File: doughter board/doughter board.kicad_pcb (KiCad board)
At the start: 2 copper layers, 36 parts, among them J1 BOOT_TO/ SELECTOR, J2 BOOT_TO/ SELECTOR, J3 Conn_01x05, J4 RS485, J5 UART2, SW1 SW_SPST, U1 LM1117-3.3, U2 SN65HVD11, U3 STM32F030C6Tx, Y1 8 MHz

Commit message: time is just a number
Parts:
- moved C7 93.6 mm to (163.2, 77.1)
- moved R6 87.0 mm to (165.5, 73.3), turned to -90 degrees
- moved R5 84.8 mm to (162.5, 73.0), turned to -90 degrees
- moved J3 84.1 mm to (147.3, 58.4), turned to 90 degrees
- moved C8 83.7 mm to (158.3, 63.5)
- moved R4 82.7 mm to (160.0, 71.1), turned to 90 degrees
- moved R12 81.6 mm to (166.2, 68.4), turned to 90 degrees
- moved R8 80.1 mm to (158.4, 76.2)
- moved R11 79.7 mm to (163.7, 68.4), turned to 90 degrees
- moved C9 78.1 mm to (153.3, 63.5)
- moved U1 77.7 mm to (165.1, 61.0)
- moved R9 77.2 mm to (160.0, 67.0), turned to 90 degrees
- moved C3 75.7 mm to (144.8, 68.7), turned to -90 degrees
- moved C10 72.6 mm to (148.2, 63.5)
- moved R2 66.0 mm to (141.2, 69.2), turned to -90 degrees
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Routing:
- net +3.3V: track 0.00 -> 42.5 mm
- net GND: track 0.00 -> 26.0 mm
- net RST: track 0.00 -> 15.6 mm, vias 0 -> 1
- net SWD_O: track 0.00 -> 13.2 mm, vias 0 -> 1
- net SWD_CLK: track 0.00 -> 12.9 mm, vias 0 -> 1
- net +5V: track 10.7 -> 0.00 mm
- net /UART2_TX: track 1.00 -> 0.00 mm
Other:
- board outline added: 61 x 27.9 mm

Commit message: PCB doughter - layout
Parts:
- moved D1 44.3 mm to (157.5, 58.4)
- moved C2 44.3 mm to (161.3, 66.0), turned to 90 degrees
- moved C5 44.1 mm to (158.4, 73.2), turned to -90 degrees
- moved J2 37.6 mm to (151.1, 66.0)
- moved C1 36.3 mm to (158.3, 64.7), turned to 90 degrees
- moved J3 34.4 mm to (113.0, 55.5)
- moved C8 33.9 mm to (124.5, 62.2)
- moved C7 33.8 mm to (137.2, 55.5), turned to 180 degrees
- moved C9 32.8 mm to (120.7, 59.7)
- moved R2 29.5 mm to (111.8, 67.3)
- moved D3 28.8 mm to (146.1, 67.3), turned to -90 degrees
- moved J4 28.7 mm to (163.8, 58.4), turned to 180 degrees
- moved R12 27.2 mm to (139.7, 62.2), turned to 180 degrees
- moved R8 25.8 mm to (139.7, 58.4), turned to 90 degrees
- moved R3 24.8 mm to (150.4, 57.9), turned to -90 degrees
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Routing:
- net +3.3V: track 42.5 -> 120.1 mm
- net GND: track 26.0 -> 1.43 mm
- net DE: track 0.00 -> 23.1 mm, vias 0 -> 2
- net RST: track 15.6 -> 38.1 mm
- net ~{RE}: track 0.00 -> 19.6 mm, vias 0 -> 2
- net UART1_RX_R: track 0.00 -> 19.1 mm, vias 0 -> 4
- net /A: track 0.00 -> 18.4 mm
- net Xtal_IN: track 0.00 -> 14.8 mm
- net UART1_TX_D: track 0.00 -> 12.4 mm, vias 0 -> 2
- net /B: track 0.00 -> 12.1 mm
- net SWD_O: track 13.2 -> 25.1 mm
- net Xtal_OUT: track 0.00 -> 11.1 mm
- net +5V: track 0.00 -> 10.2 mm
- net SWD_CLK: track 12.9 -> 22.2 mm
- net Net-(U2-B): track 0.00 -> 8.62 mm
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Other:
- board size 61 x 27.9 mm -> 58.4 x 24.1 mm

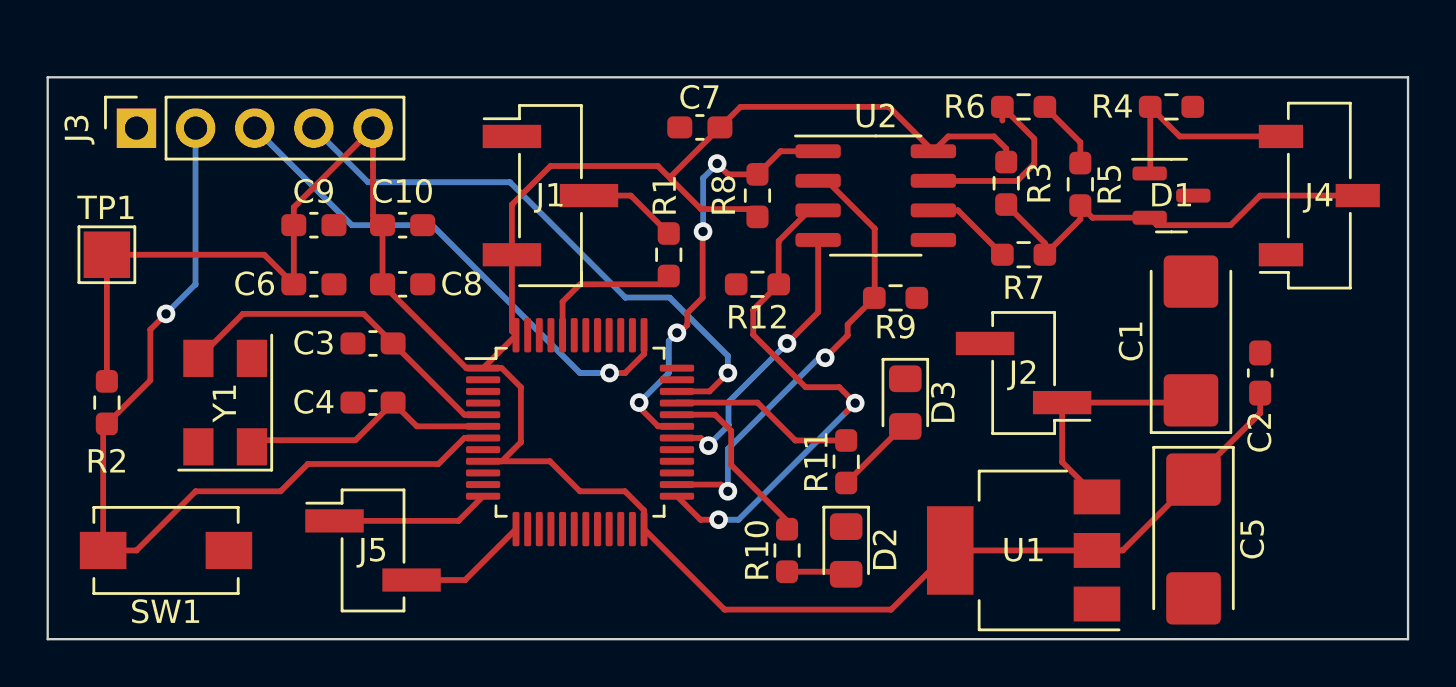
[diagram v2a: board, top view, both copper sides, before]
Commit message: doughter PCB - with no GND connection
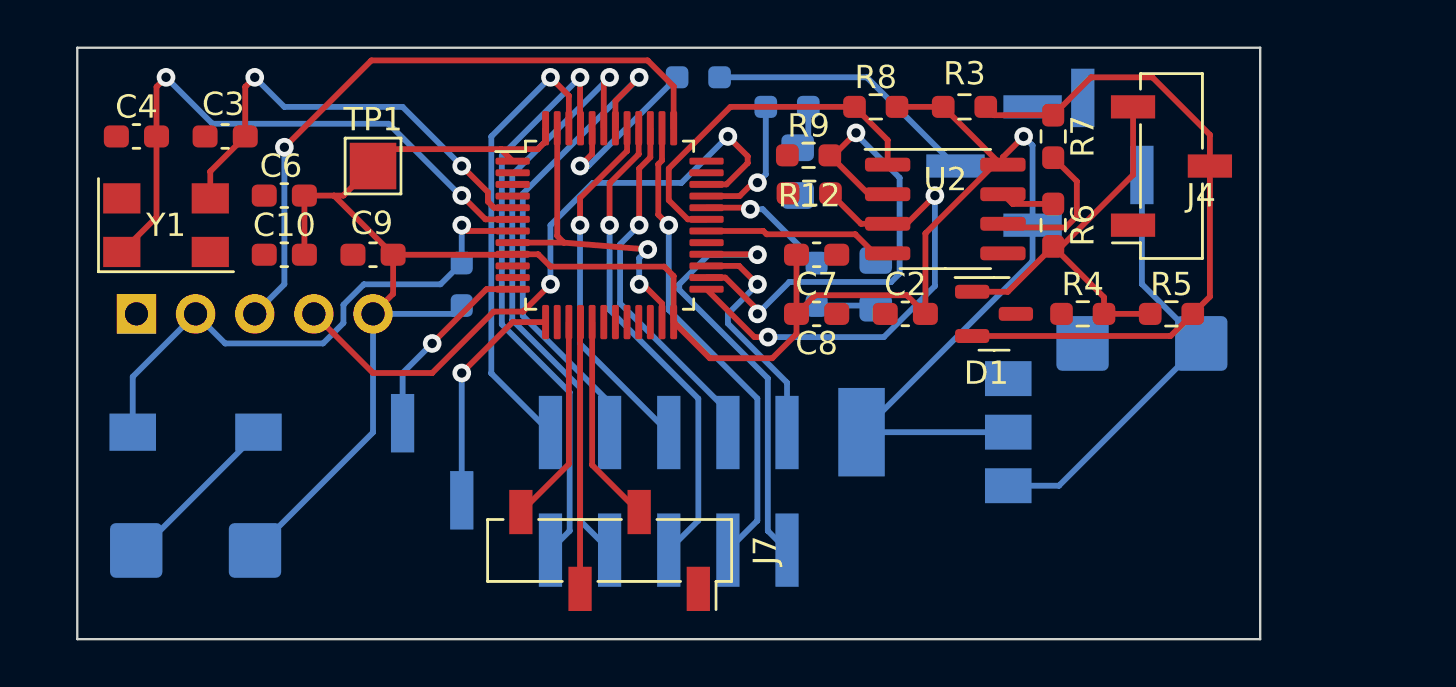
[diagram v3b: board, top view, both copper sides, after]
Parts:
- added J6: INPUT, Connector_PinHeader_2.54mm:PinHeader_2x05_P2.54mm_Vertical_SMD, B.Cu at (135.9, 71.1)
- added J7: Serial_BUS, Connector_PinSocket_2.54mm:PinSocket_1x04_P2.54mm_Vertical_SMD_Pin1Right, F.Cu at (133.3, 73.7)
- C1, C5, D2, D3, J1, J2, J3, J5, R1, R10, R11, R2, SW1, U1: moved to B.Cu
- moved C5 42.9 mm to (115.6, 73.7), turned to 180 degrees
- moved J1 19.1 mm to (149.9, 57.1), turned to 180 degrees
- moved C8 17.8 mm to (142.2, 63.5)
- moved R2 16.1 mm to (127.0, 62.2), turned to 90 degrees
- moved R11 15.5 mm to (141.0, 54.6), turned to 0 degrees
- moved C2 15.5 mm to (146.1, 63.5), turned to 180 degrees
- moved C4 15.3 mm to (113.0, 55.9)
- moved TP1 12.0 mm to (123.2, 57.1)
- moved D2 11.5 mm to (144.8, 62.2)
- moved R10 11.5 mm to (142.2, 62.2)
- moved D3 10.9 mm to (141.4, 57.4), turned to 90 degrees
- moved C3 10.9 mm to (116.8, 55.9)
- moved J2 10.9 mm to (154.9, 55.9), turned to 90 degrees
- moved R4 9.67 mm to (153.7, 63.5), turned to 180 degrees
- moved D1 9.16 mm to (149.9, 63.5)
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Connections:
- U3 pad 23: unconnected-(U3-VSS-Pad23) -> Net-(U3-VSSA)
- U3 pad 47: unconnected-(U3-VSS-Pad47) -> Net-(U3-VSSA)
- U3 pad 8: unconnected-(U3-VSSA-Pad8) -> Net-(U3-VSSA)
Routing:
- net /Col1: track 0.00 -> 26.1 mm, vias 0 -> 1
- net /Col2: track 0.00 -> 25.5 mm, vias 0 -> 1
- net /Col0: track 0.00 -> 21.5 mm, vias 0 -> 1
- net /Col4: track 0.00 -> 20.7 mm, vias 0 -> 1
- net /Col7: track 0.00 -> 20.5 mm, vias 0 -> 1
- net /Col3: track 0.00 -> 19.9 mm, vias 0 -> 1
- net /Col9: track 0.00 -> 19.4 mm, vias 0 -> 1
- net /Col6: track 0.00 -> 16.6 mm, vias 0 -> 1
- net /Col5: track 0.00 -> 15.5 mm, vias 0 -> 1
- net Xtal_OUT: track 11.1 -> 25.9 mm, vias 0 -> 2
- net Net-(U3-VSSA): track 0.00 -> 14.6 mm, vias 0 -> 2
- net +3.3V: track 120.1 -> 105.6 mm, vias 0 -> 1
- net RST: track 38.1 -> 24.0 mm
- net /S_LE: track 0.00 -> 11.5 mm
- net /A: track 18.4 -> 29.3 mm
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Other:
- board size 58.4 x 24.1 mm -> 50.8 x 25.4 mm

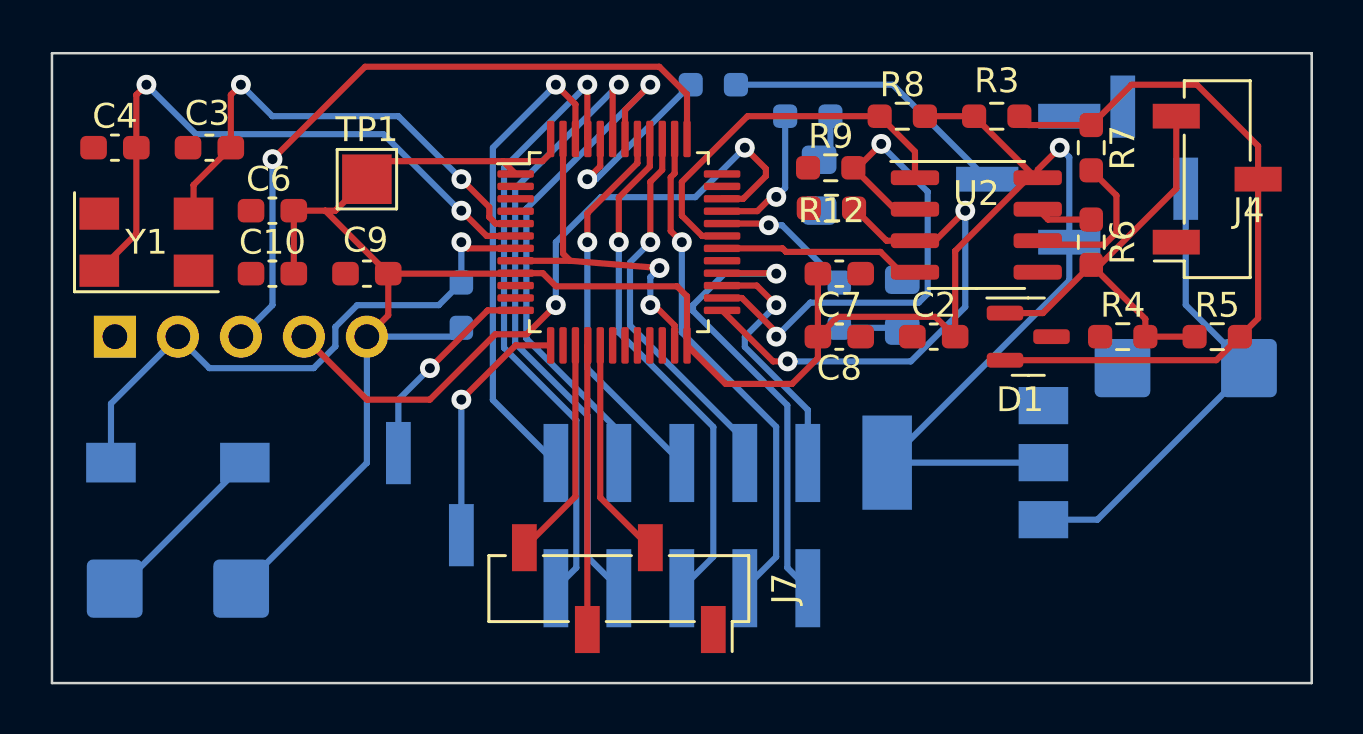
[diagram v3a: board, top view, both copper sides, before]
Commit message: Modified layout, filled GND planes, added info on silkscreen
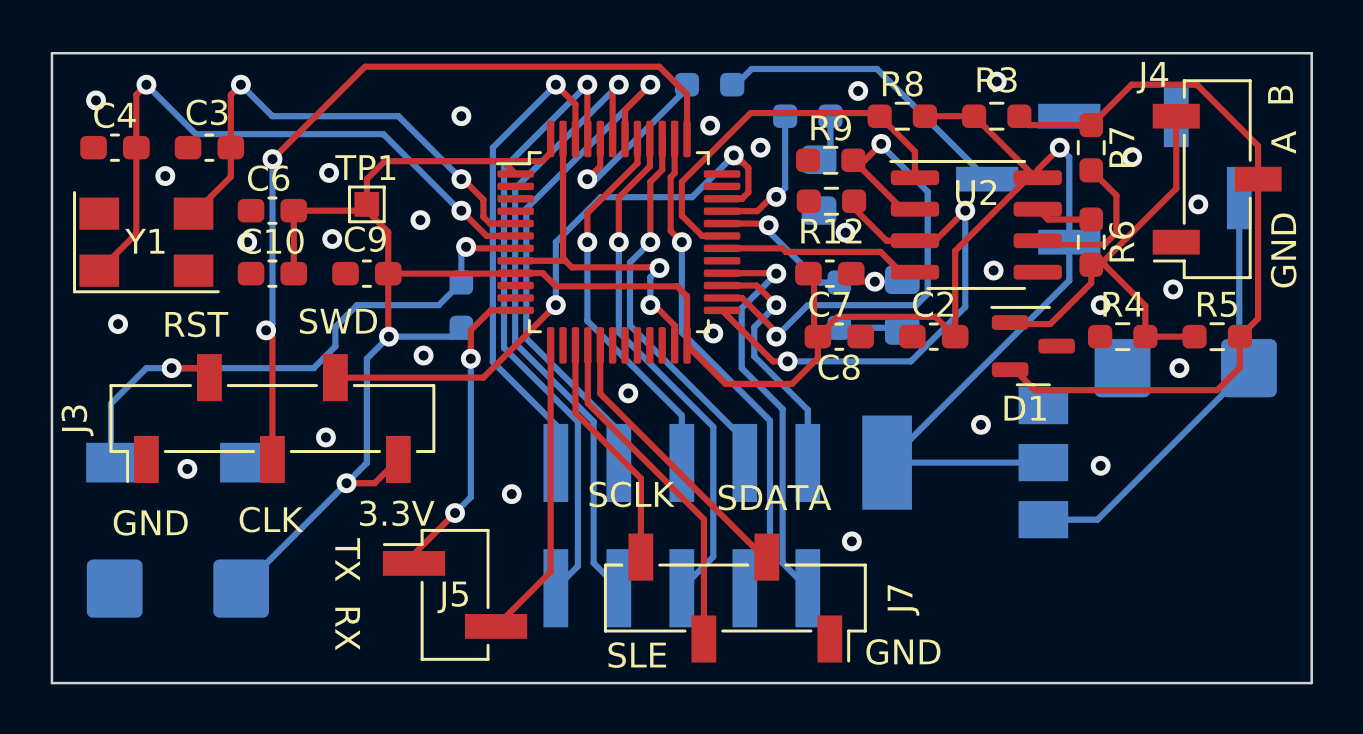
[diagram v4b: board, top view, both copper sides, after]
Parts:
- J3: footprint Connector_PinSocket_2.54mm:PinSocket_1x05_P2.54mm_Vertical -> Connector_PinSocket_2.54mm:PinSocket_1x05_P2.54mm_Vertical_SMD_Pin1Left; moved to F.Cu
- J5: moved to F.Cu
- J6: value INPUT -> OUTPUT
- TP1: footprint TestPoint:TestPoint_Pad_2.0x2.0mm -> TestPoint:TestPoint_Pad_1.0x1.0mm
- moved J3 7.16 mm to (119.4, 66.8), turned to 90 degrees
- moved J7 4.71 mm to (138.0, 74.0)
- moved J5 4.19 mm to (126.7, 73.9), turned to 0 degrees
- moved J2 2.19 mm to (157.1, 56.3)
- moved TP1 1.02 mm to (123.2, 58.2)
- moved D1 0.43 mm to (150.1, 63.9)
- moved C7 0.38 mm to (141.9, 61.0)
- moved R9 0.30 mm to (141.9, 56.4)
- moved R12 0.28 mm to (141.9, 58.0)
- moved R1 0.15 mm to (137.0, 53.3)
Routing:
- net GND: track 7.35 -> 1.82 mm, vias 0 -> 29
- net SWD_CLK: track 28.2 -> 32.8 mm, vias 1 -> 2
- net /UART2_TX: track 8.37 -> 12.5 mm, vias 1 -> 2
- net SWD_O: track 28.2 -> 24.4 mm
- net /Col9: track 19.4 -> 16.6 mm
- net /S_DATA: track 8.99 -> 11.4 mm
- net /S_LE: track 11.5 -> 13.8 mm
- net /UART2_RX: track 9.97 -> 12.2 mm, vias 1 -> 0
- net +3.3V: track 105.6 -> 107.4 mm, vias 1 -> 3
- net +5V: track 19.1 -> 17.8 mm
- net /A: track 29.3 -> 30.5 mm
- net /S_CLK: track 9.01 -> 9.63 mm
- net Net-(J1-Pin_2): track 11.7 -> 12.2 mm
- net RST: track 24.0 -> 24.2 mm, vias 1 -> 2
- added copper zone on B.Cu, net GND
- added copper zone on F.Cu, net GND
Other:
- board text added: "1"
- board text added: "10"
- board text added: "2"
- board text added: "3"
- board text added: "3.3V"
- board text added: "4"
- board text added: "5"
- board text added: "5V"
- board text added: "6"
- board text added: "7"
- board text added: "8"
- board text added: "9"
- board text added: "A"
- board text added: "B"
- board text added: "BOOT0"
- board text added: "CLK"
- board text added: "COLUMNS"
- board text added: "GND"
- board text added: "RST"
- board text added: "RX"
- board text added: "SCLK"
- board text added: "SDATA"
- board text added: "SLE"
- board text added: "SWD"
- board text added: "TX"

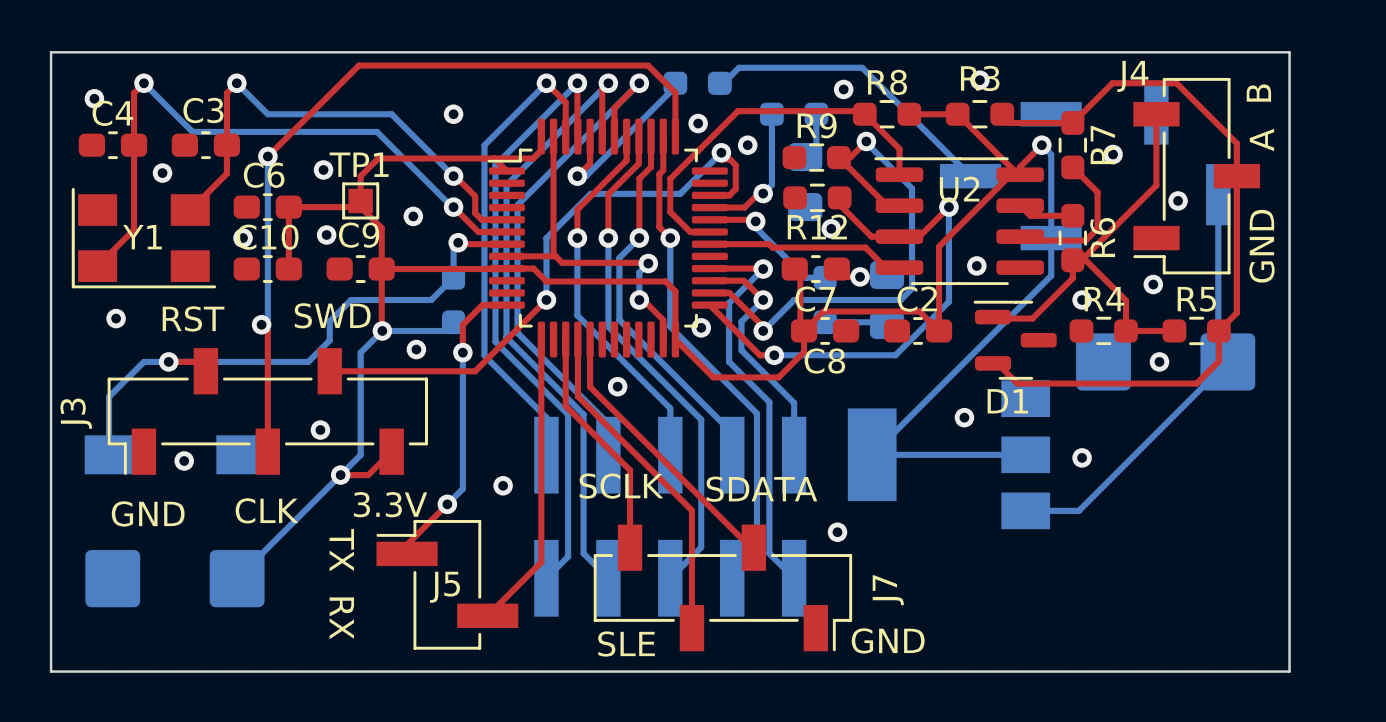
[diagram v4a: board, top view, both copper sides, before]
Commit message: finished pcb, except copper slab
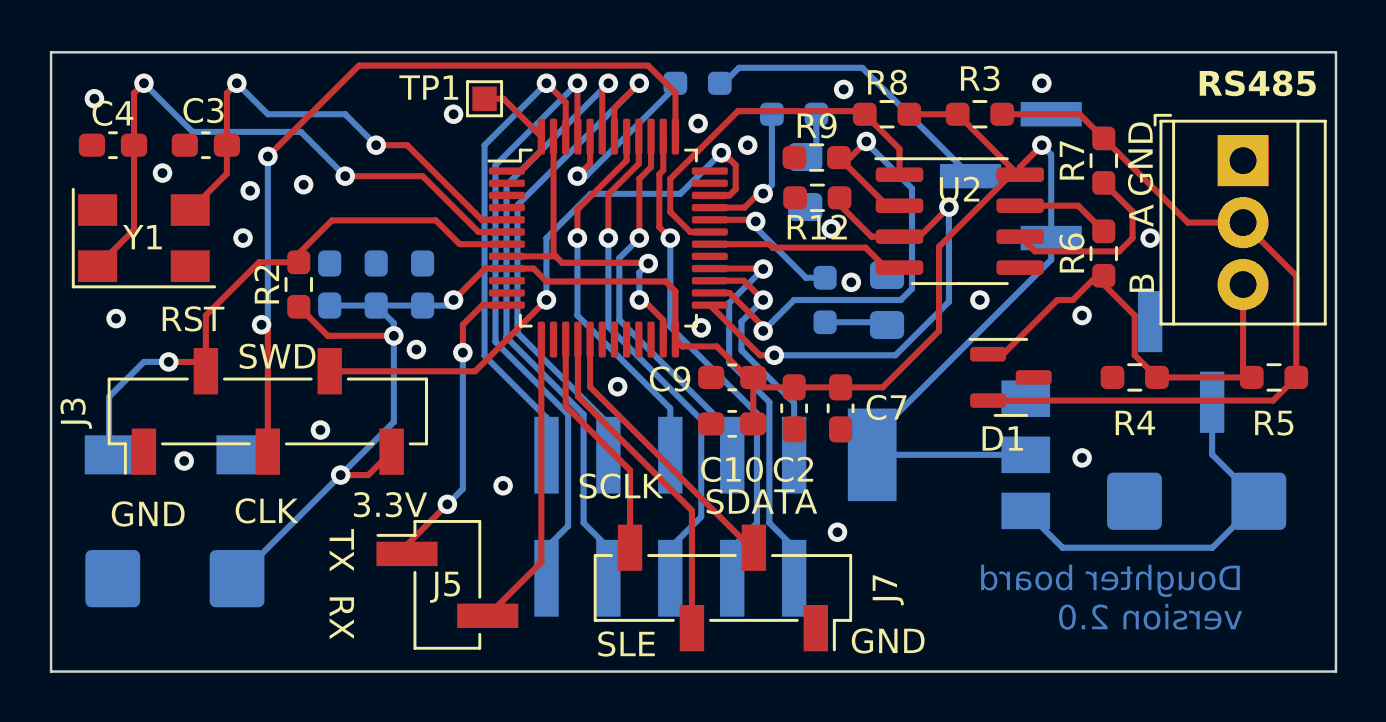
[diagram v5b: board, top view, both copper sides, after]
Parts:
- added C11: 4.7u, Capacitor_SMD:C_0603_1608Metric_Pad1.08x0.95mm_HandSolder, B.Cu at (125.7, 61.6)
- C10: value 100n -> 10n
- C6, C8: moved to B.Cu
- C9: value 100n -> 1u
- J4: value RS485 -> RS 485; footprint Connector_PinSocket_2.54mm:PinSocket_1x03_P2.54mm_Vertical_SMD_Pin1Right -> TerminalBlock_TE-Connectivity:TerminalBlock_TE_282834-3_1x03_P2.54mm_Horizontal
- R2: moved to F.Cu
- moved C8 20.4 mm to (121.9, 61.6), turned to 90 degrees
- moved C10 20.1 mm to (138.4, 67.3)
- moved C9 15.9 mm to (138.4, 65.4)
- moved J2 8.52 mm to (156.8, 64.8)
- moved TP1 6.59 mm to (128.3, 54.0)
- moved R2 6.38 mm to (120.7, 61.6)
- moved C2 5.99 mm to (141.0, 66.7), turned to -90 degrees
- moved C1 5.85 mm to (157.5, 70.5)
- moved C7 5.80 mm to (142.9, 66.7), turned to -90 degrees
- moved C6 5.46 mm to (123.8, 61.6), turned to 90 degrees
- moved R5 3.70 mm to (160.7, 65.4)
- moved R4 2.29 mm to (154.9, 65.4)
- moved J4 2.01 mm to (159.4, 56.5), turned to -90 degrees
- moved D1 1.54 mm to (149.9, 65.4)
- moved R6 1.42 mm to (153.7, 60.3)
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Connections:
- C10 pad 1: +3.3V -> VDD
- C2 pad 1: +3.3V -> VDD
- C5 pad 1: +3.3V -> VDD
- C6 pad 1: +3.3V -> VDD
- C7 pad 1: +3.3V -> VDD
- C8 pad 1: +3.3V -> VDD
- C9 pad 1: +3.3V -> VDD
- J1 pad 3: +3.3V -> VDD
- J3 pad 5: +3.3V -> VDD
- R2 pad 1: +3.3V -> VDD
- R3 pad 1: +3.3V -> VDD
- R8 pad 1: +3.3V -> VDD
- TP1 pad 1: +3.3V -> Net-(TP1-Pad1)
- U1 pad 2: +3.3V -> VDD
- U1 pad 4: +3.3V -> VDD
- U2 pad 8: +3.3V -> VDD
- U3 pad 1: +3.3V -> Net-(TP1-Pad1)
- U3 pad 24: +3.3V -> VDD
- U3 pad 48: +3.3V -> Net-(TP1-Pad1)
- U3 pad 9: +3.3V -> VDD
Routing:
- net +3.3V: track 107.4 -> 0.00 mm, vias 3 -> 0
- net VDD: track 0.00 -> 90.1 mm, vias 0 -> 4
- net Net-(TP1-Pad1): track 0.00 -> 5.30 mm
- net +5V: track 17.8 -> 15.8 mm
- net GND: track 1.82 -> 0.17 mm, vias 29 -> 24
- net Net-(U2-B): track 2.33 -> 3.86 mm
- net /A: track 30.5 -> 32.0 mm
- net Net-(U2-A): track 6.37 -> 7.84 mm
- net /B: track 18.2 -> 19.0 mm
- net RST: track 24.2 -> 23.4 mm, vias 2 -> 1
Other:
- board size 50.8 x 25.4 mm -> 52.7 x 25.4 mm
- board text added: "Doughter board version 2.0"
- board text added: "RS485"
